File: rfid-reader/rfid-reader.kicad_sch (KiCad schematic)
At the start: 10 parts, among them U1 ATmega1284-P, U2 keypad, U3 Interface_RFID_SPI

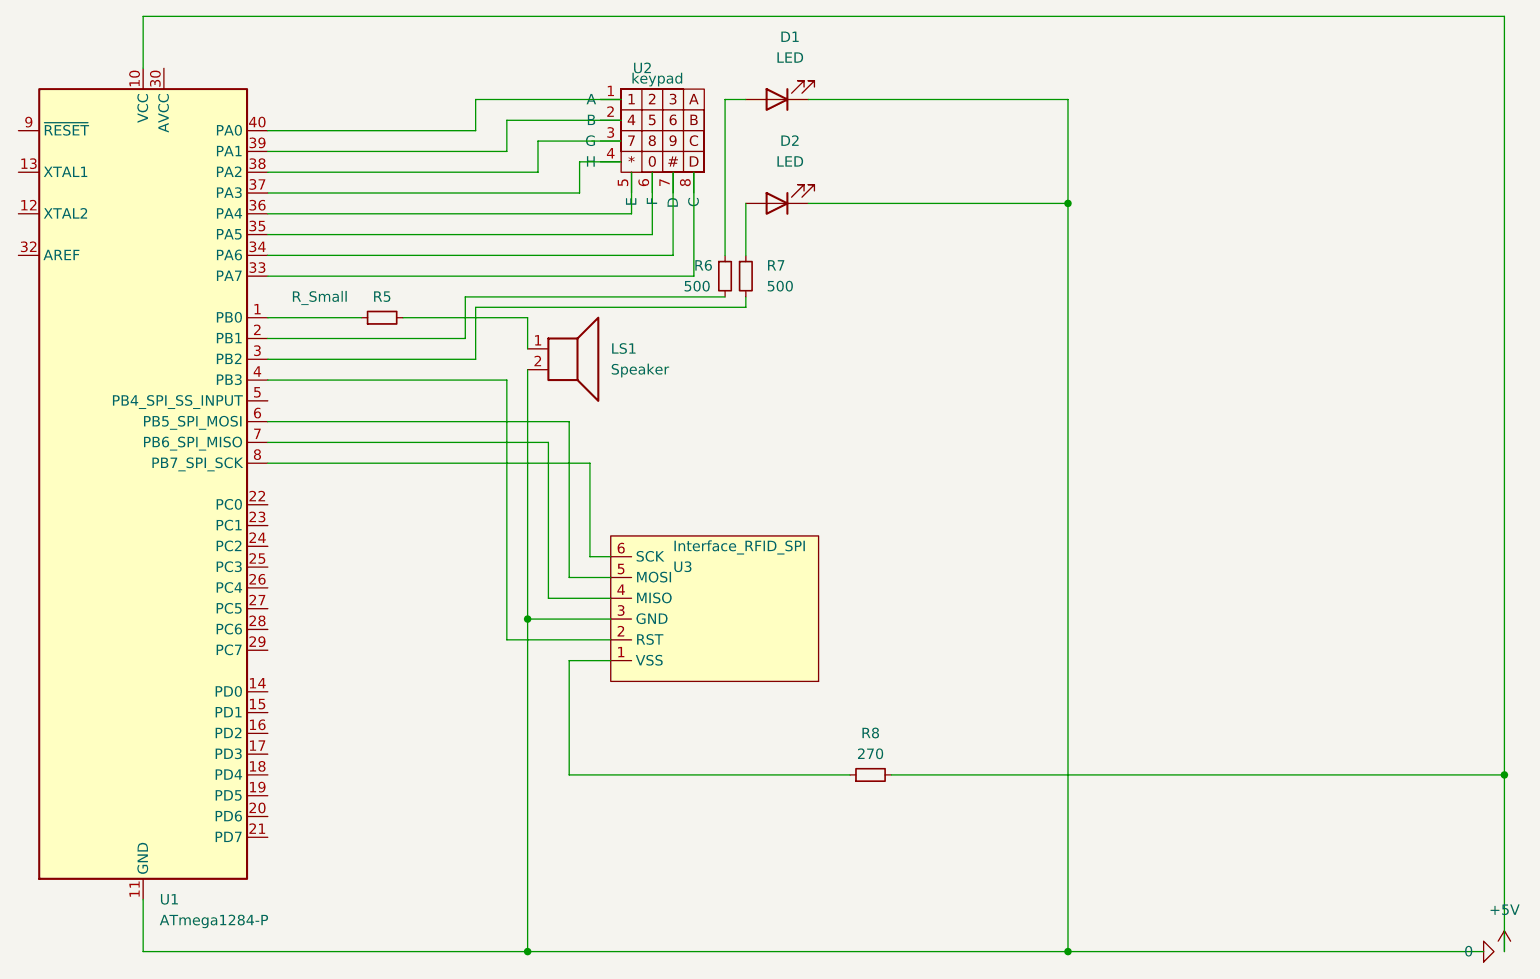
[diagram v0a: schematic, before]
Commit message: Add pull-down resistors to keypad buttons
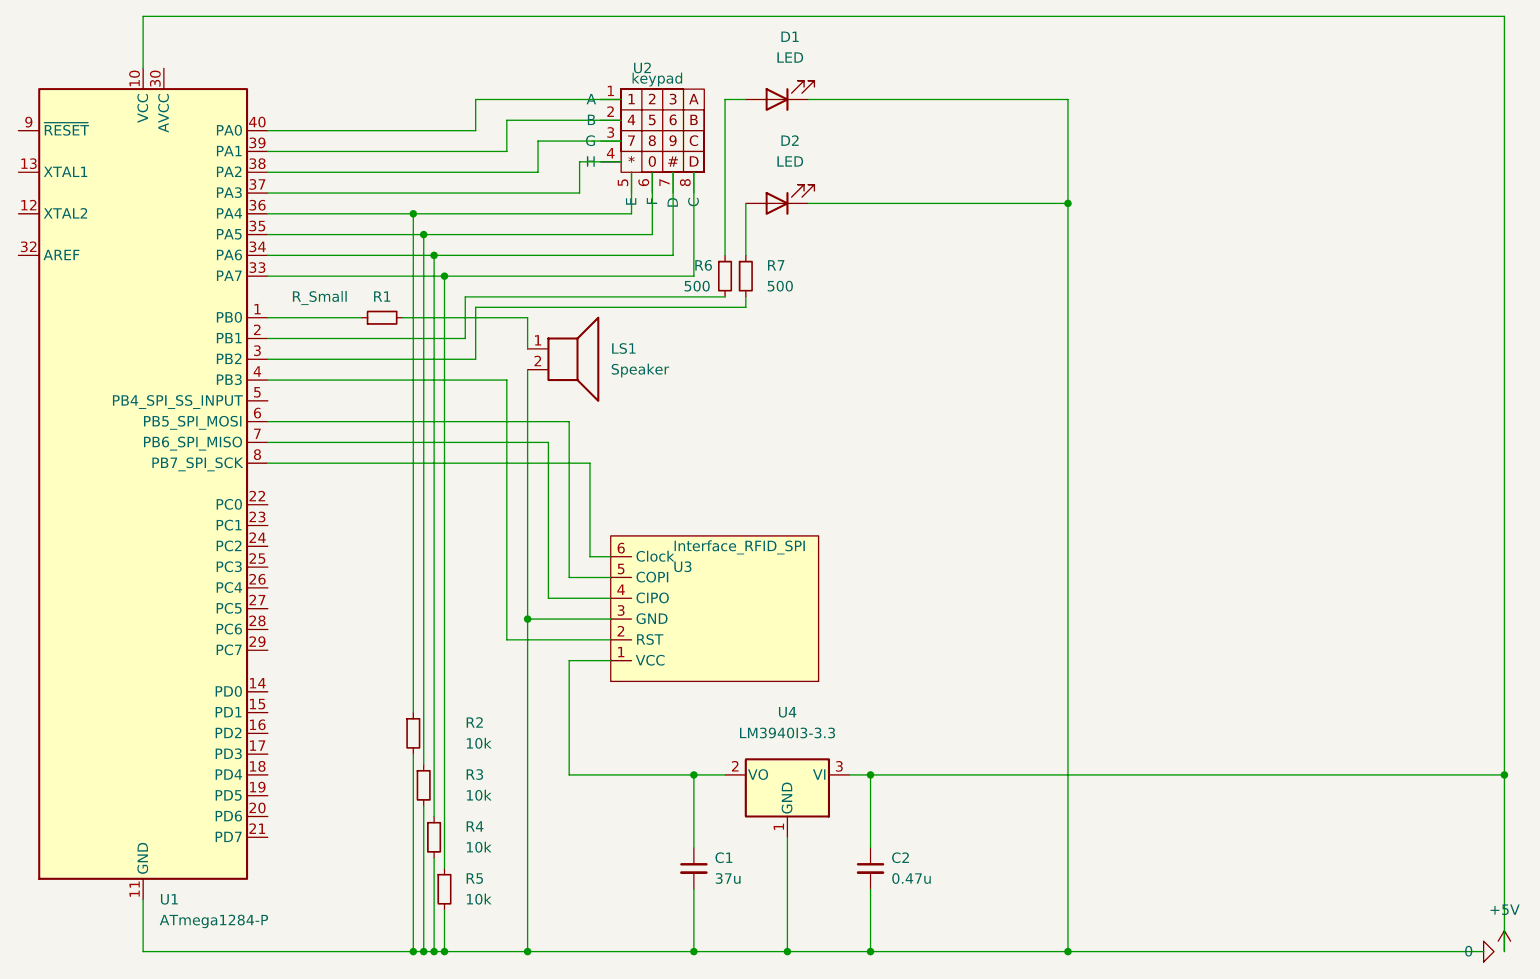
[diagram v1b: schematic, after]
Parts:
- removed R8: 270, symbol Device:R_Small
- added C1: 37u, symbol Device:C_Small
- added C2: 0.47u, symbol Device:C_Small
- added R2, R3, R4, R5: 10k, symbol Device:R_Small
- added U4: LM3940I3-3.3, symbol Regulator_Linear:LM1117-3.3
- renumbered R5 to R1
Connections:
- net +5V: now also C2.1, U4.3 (VI)
- net 0: now also C1.2, C2.2, R2.2, R3.2, R4.2, R5.2, U4.1 (GND)
- net at U1.36 (PA4), U2.5 (E): now also R2.1
- net at U1.35 (PA5), U2.6 (F): now also R3.1
- net at U1.34 (PA6), U2.7 (D): now also R4.1
- net at U1.33 (PA7), U2.8 (C): now also R5.1
- net at U3.1 (VCC): now also C1.1, U4.2 (VO)
